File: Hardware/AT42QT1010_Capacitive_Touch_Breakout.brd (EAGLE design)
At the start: 25.4 x 33 mm, 28 parts, among them Q1 600mA/40V, U1 AT42QT1010 - UDFN

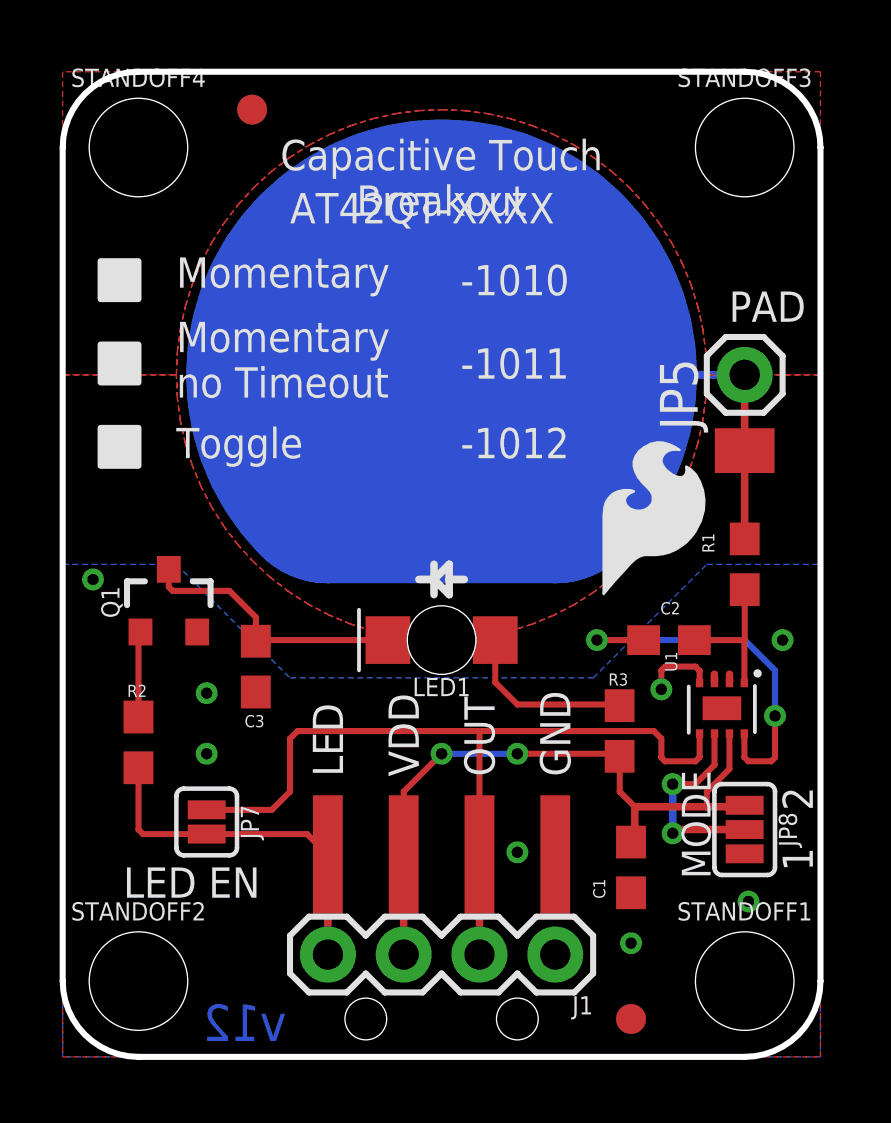
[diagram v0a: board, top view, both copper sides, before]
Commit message: Issues from double check Fixed
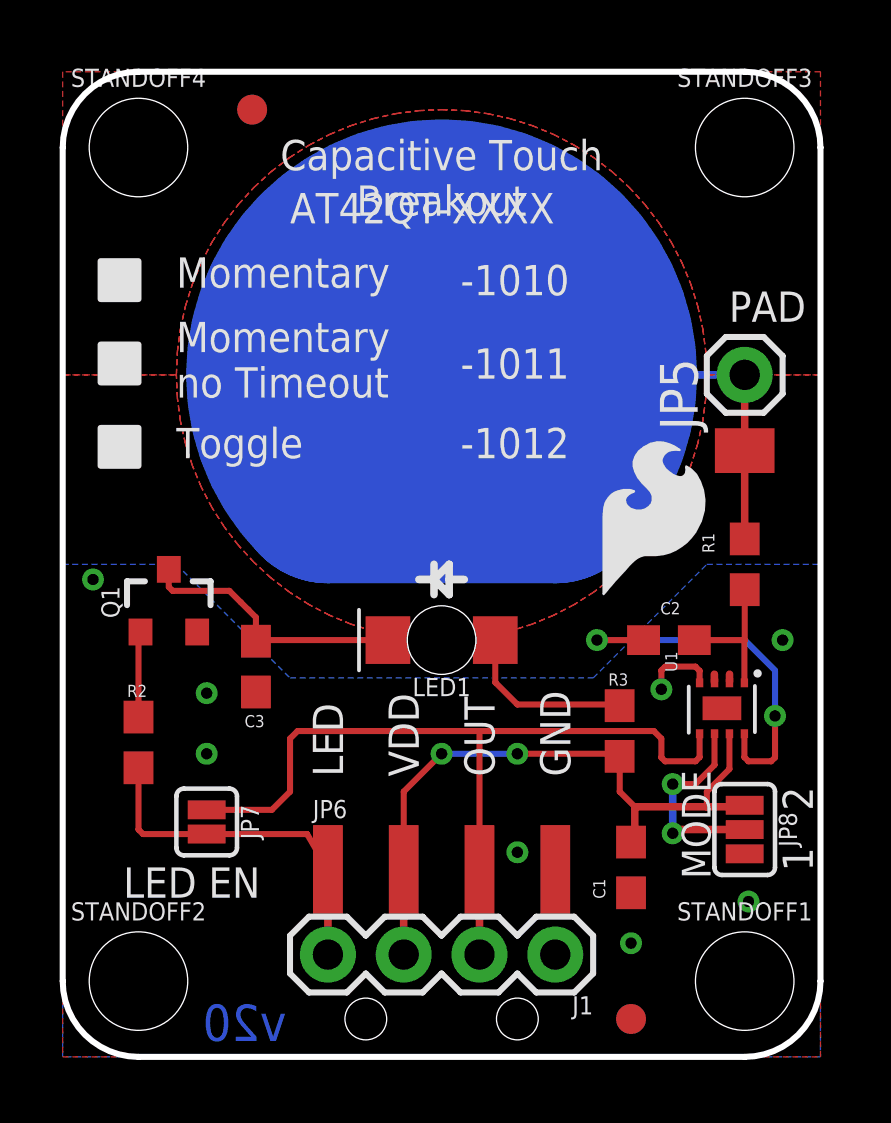
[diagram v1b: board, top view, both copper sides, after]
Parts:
- JP6: device SparkFun-Connectors:1X04_SMD_LONG -> SparkFun-Connectors:1X04_SMD_RA_MALE
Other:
- board text added: "v20"
- board text removed: "v12"
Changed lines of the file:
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@@
 <layer number="20" name="Dimension" color="15" fill="1" visible="yes" active="yes"/>
 <layer number="21" name="tPlace" color="16" fill="1" visible="yes" active="yes"/>
-<layer number="22" name="bPlace" color="14" fill="1" visible="no" active="yes"/>
+<layer number="22" name="bPlace" color="14" fill="1" visible="yes" active="yes"/>
 <layer number="23" name="tOrigins" color="15" fill="1" visible="yes" active="yes"/>
 <layer number="24" name="bOrigins" color="15" fill="1" visible="yes" active="yes"/>
@@
 <layer number="47" name="Measures" color="7" fill="1" visible="no" active="yes"/>
 <layer number="48" name="Document" color="7" fill="1" visible="no" active="yes"/>
-<layer number="49" name="Reference" color="7" fill="1" visible="yes" active="yes"/>
+<layer number="49" name="Reference" color="7" fill="1" visible="no" active="yes"/>
 <layer number="50" name="dxf" color="7" fill="1" visible="no" active="yes"/>
 <layer number="53" name="tGND_GNDA" color="7" fill="9" visible="no" active="no"/>
@@
 <text x="13.97" y="5.08" size="1.016" layer="22" font="vector" ratio="15" rot="MR270" align="center-right">OUT</text>
 <text x="16.51" y="5.08" size="1.016" layer="22" font="vector" ratio="15" rot="MR270" align="center-right">GND</text>
-<text x="6.096" y="1.143" size="1.2192" layer="16" font="vector" ratio="15" rot="MR0" align="center">v12</text>
+<text x="6.096" y="1.143" size="1.2192" layer="16" font="vector" ratio="15" rot="MR0" align="center">v20</text>
 <text x="22.86" y="24.638" size="1.016" layer="22" font="vector" ratio="15" rot="MR270" align="center-right">PAD</text>
 <text x="12.7" y="28.194" size="1.016" layer="21" font="vector" ratio="19" align="bottom-center">Capacitive Touch
@@
 <attribute name="VALUE" x="21.59" y="19.685" size="1.27" layer="27"/>
 </element>
-<element name="JP6" library="SparkFun-Connectors" package="1X04_SMD_LONG" value="SMD" x="12.7" y="1.27">
+<element name="JP6" library="SparkFun-Connectors" package="1X04_SMD_RA_MALE" value="SMD" x="12.7" y="1.27">
 <attribute name="SF_ID" value="PRT-12638" x="12.7" y="1.27" size="1.778" layer="27" display="off"/>
 <attribute name="PROD_ID" value="CONN-09140" x="12.7" y="1.27" size="1.778" layer="27" display="off"/>
@@
 <wire x1="22.8092" y1="8.382" x2="22.86" y2="8.4328" width="0.254" layer="1"/>
 <contactref element="J1" pad="3"/>
-<wire x1="11.43" y1="3.429" x2="11.43" y2="6.77" width="0.254" layer="1"/>
+<wire x1="11.43" y1="3.429" x2="11.43" y2="6.27" width="0.254" layer="1"/>
 <wire x1="21.59" y1="8.89" x2="21.59" y2="8.382" width="0.2032" layer="1"/>
 <wire x1="18.669" y1="10.072" x2="18.669" y2="8.89" width="0.2032" layer="1"/>
-<wire x1="11.43" y1="6.77" x2="11.43" y2="8.89" width="0.2032" layer="1"/>
+<wire x1="11.43" y1="6.27" x2="11.43" y2="8.89" width="0.2032" layer="1"/>
 <wire x1="11.43" y1="8.89" x2="12.7" y2="10.16" width="0.2032" layer="1"/>
 <via x="12.7" y="10.16" extent="1-16" drill="0.381"/>
@@
 <contactref element="JP7" pad="1"/>
 <contactref element="J1" pad="2"/>
-<wire x1="13.97" y1="6.77" x2="13.97" y2="3.429" width="0.254" layer="1"/>
+<wire x1="13.97" y1="6.27" x2="13.97" y2="3.429" width="0.254" layer="1"/>
 <wire x1="4.826" y1="8.2804" x2="7.0104" y2="8.2804" width="0.2032" layer="1"/>
 <wire x1="7.62" y1="8.89" x2="7.62" y2="10.668" width="0.2032" layer="1"/>
-<wire x1="13.97" y1="10.922" x2="13.97" y2="6.77" width="0.2032" layer="1"/>
+<wire x1="13.97" y1="10.922" x2="13.97" y2="6.27" width="0.2032" layer="1"/>
 <wire x1="19.812" y1="10.922" x2="13.97" y2="10.922" width="0.2032" layer="1"/>
 <wire x1="7.62" y1="10.668" x2="7.874" y2="10.922" width="0.2032" layer="1"/>
@@
 <contactref element="J1" pad="4"/>
 <wire x1="8.89" y1="3.81" x2="8.89" y2="3.429" width="0.254" layer="16"/>
-<wire x1="8.89" y1="6.77" x2="8.89" y2="3.429" width="0.254" layer="1"/>
-<wire x1="8.6224" y1="6.5024" x2="8.89" y2="6.77" width="0.2032" layer="1"/>
+<wire x1="8.89" y1="6.27" x2="8.89" y2="3.429" width="0.254" layer="1"/>
+<wire x1="8.6224" y1="6.5024" x2="8.89" y2="6.27" width="0.2032" layer="1"/>
 <wire x1="4.6736" y1="7.62" x2="4.826" y2="7.4676" width="0.2032" layer="1"/>
 <wire x1="4.826" y1="7.4676" x2="2.6924" y2="7.4676" width="0.2032" layer="1"/>
@@
 <wire x1="2.54" y1="7.62" x2="2.54" y2="9.691" width="0.2032" layer="1"/>
 <wire x1="4.826" y1="7.4676" x2="8.1924" y2="7.4676" width="0.2032" layer="1"/>
-<wire x1="8.1924" y1="7.4676" x2="8.89" y2="6.77" width="0.2032" layer="1"/>
+<wire x1="8.1924" y1="7.4676" x2="8.89" y2="6.27" width="0.2032" layer="1"/>
 </signal>
 <signal name="N$4">

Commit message: Update for REDS review
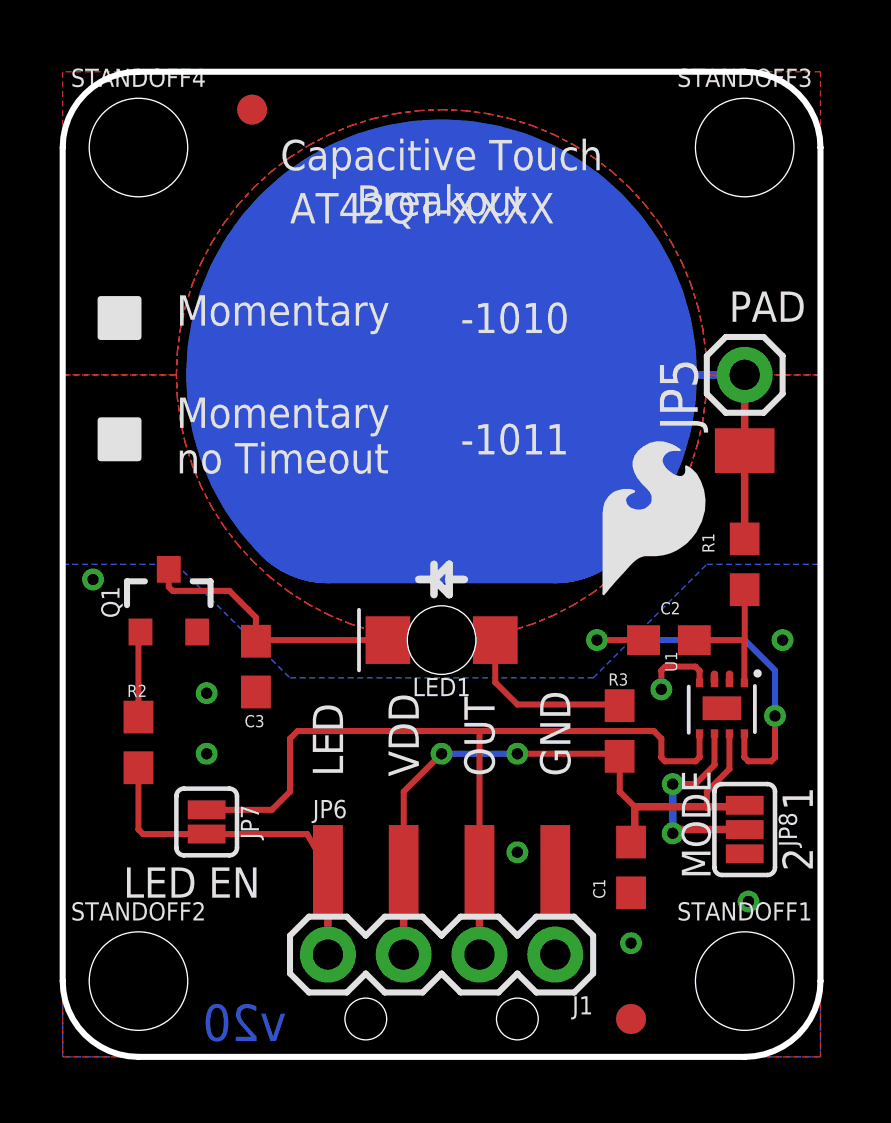
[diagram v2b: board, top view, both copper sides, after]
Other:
- board text removed: "-1012"
- board text removed: "Toggle"
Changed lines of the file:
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@@
 <layer number="47" name="Measures" color="7" fill="1" visible="no" active="yes"/>
 <layer number="48" name="Document" color="7" fill="1" visible="no" active="yes"/>
-<layer number="49" name="Reference" color="7" fill="1" visible="no" active="yes"/>
+<layer number="49" name="Reference" color="7" fill="1" visible="yes" active="yes"/>
 <layer number="50" name="dxf" color="7" fill="1" visible="no" active="yes"/>
 <layer number="53" name="tGND_GNDA" color="7" fill="9" visible="no" active="no"/>
@@
 <rectangle x1="21.971" y1="14.351" x2="22.352" y2="14.859" layer="41"/>
 <rectangle x1="7.62" y1="7.874" x2="8.001" y2="8.382" layer="41"/>
-<text x="3.81" y="25.781" size="1.016" layer="21" font="vector" ratio="15">Momentary</text>
-<text x="3.81" y="20.066" size="1.016" layer="21" font="vector" ratio="15">Toggle</text>
-<text x="3.81" y="22.098" size="1.016" layer="21" font="vector" ratio="15">Momentary
+<text x="3.81" y="24.511" size="1.016" layer="21" font="vector" ratio="15">Momentary</text>
+<text x="3.81" y="19.558" size="1.016" layer="21" font="vector" ratio="15">Momentary
 no Timeout</text>
-<text x="13.335" y="22.733" size="1.016" layer="21" font="vector" ratio="15">-1011</text>
-<text x="13.335" y="25.527" size="1.016" layer="21" font="vector" ratio="15">-1010</text>
-<text x="13.335" y="20.066" size="1.016" layer="21" font="vector" ratio="15">-1012</text>
+<text x="13.335" y="20.193" size="1.016" layer="21" font="vector" ratio="15">-1011</text>
+<text x="13.335" y="24.257" size="1.016" layer="21" font="vector" ratio="15">-1010</text>
 <text x="7.62" y="27.94" size="1.016" layer="21" font="vector" ratio="15">AT42QT-XXXX</text>
 <text x="21.717" y="5.969" size="0.9652" layer="21" font="vector" ratio="15" rot="R90">MODE</text>
-<text x="25.146" y="6.223" size="1.016" layer="21" font="vector" ratio="15" rot="R90">1</text>
-<text x="25.146" y="8.255" size="1.016" layer="21" font="vector" ratio="15" rot="R90">2</text>
+<text x="25.146" y="8.255" size="1.016" layer="21" font="vector" ratio="15" rot="R90">1</text>
+<text x="25.146" y="6.223" size="1.016" layer="21" font="vector" ratio="15" rot="R90">2</text>
 <polygon width="0.2032" layer="21">
-<vertex x="1.27" y="26.67"/>
 <vertex x="1.27" y="25.4"/>
+<vertex x="1.27" y="24.13"/>
+<vertex x="2.54" y="24.13"/>
 <vertex x="2.54" y="25.4"/>
-<vertex x="2.54" y="26.67"/>
 </polygon>
 <polygon width="0.2032" layer="21">
-<vertex x="1.27" y="23.876"/>
-<vertex x="1.27" y="22.606"/>
-<vertex x="2.54" y="22.606"/>
-<vertex x="2.54" y="23.876"/>
-</polygon>
-<polygon width="0.2032" layer="21">
-<vertex x="1.27" y="21.082"/>
-<vertex x="1.27" y="19.812"/>
-<vertex x="2.54" y="19.812"/>
-<vertex x="2.54" y="21.082"/>
+<vertex x="1.27" y="21.336"/>
+<vertex x="1.27" y="20.066"/>
+<vertex x="2.54" y="20.066"/>
+<vertex x="2.54" y="21.336"/>
 </polygon>
 </plain>

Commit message: Minor adjustment before double check
Moved fiducials so that it does not overlay silk, adjusted the "PAD"
silk to be better aligned with the through hole.
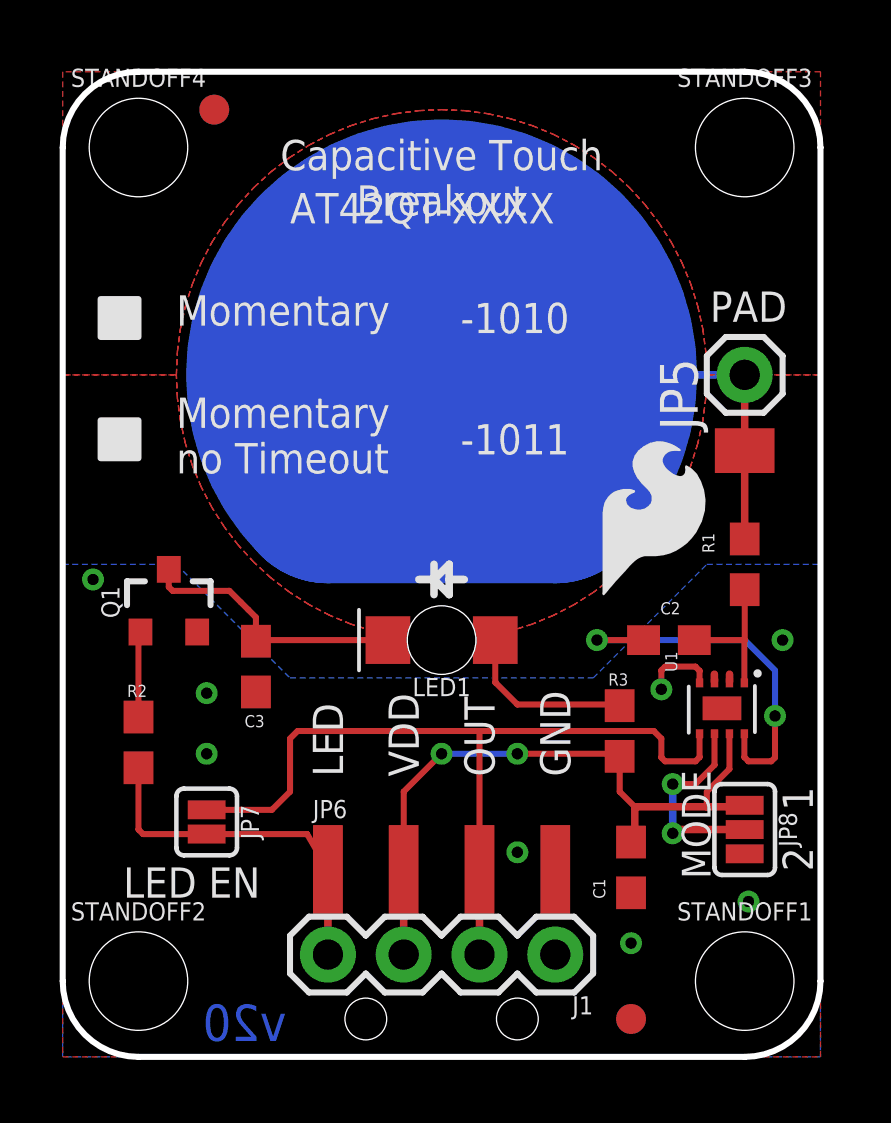
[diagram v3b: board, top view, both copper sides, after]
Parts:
- moved FID1 1.27 mm to (5.08, 31.8)
- moved FID4 1.27 mm to (5.08, 31.8)
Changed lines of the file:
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@@
 <rectangle x1="0" y1="30.48" x2="2.54" y2="33.02" layer="41"/>
 <rectangle x1="22.86" y1="30.48" x2="25.4" y2="33.02" layer="41"/>
-<text x="23.622" y="24.638" size="1.016" layer="21" font="vector" ratio="19" rot="R180" align="top-center">PAD</text>
+<text x="22.987" y="24.638" size="1.016" layer="21" font="vector" ratio="19" rot="R180" align="top-center">PAD</text>
 <text x="8.89" y="9.398" size="1.016" layer="21" font="vector" ratio="15" rot="R90" align="center-left">LED</text>
 <text x="11.43" y="9.398" size="1.016" layer="21" font="vector" ratio="15" rot="R90" align="center-left">VDD</text>
@@
 <attribute name="VALUE" value="Green" x="12.7" y="13.97" size="1.778" layer="27" rot="R180" display="off"/>
 </element>
-<element name="FID1" library="SparkFun-Aesthetics" package="FIDUCIAL-1X2" value="FIDUCIAL1X2" x="6.35" y="31.75"/>
+<element name="FID1" library="SparkFun-Aesthetics" package="FIDUCIAL-1X2" value="FIDUCIAL1X2" x="5.08" y="31.75"/>
 <element name="FID2" library="SparkFun-Aesthetics" package="FIDUCIAL-1X2" value="FIDUCIAL1X2" x="19.05" y="1.27"/>
 <element name="JP9" library="SparkFun-Connectors" package="PAD-1.5X4.5" value="M01SMD-4.5X1.5" x="22.86" y="20.32" smashed="yes" rot="R90"/>
 <element name="JP8" library="SparkFun-Jumpers" package="SMT-JUMPER_3_NO_SILK" value="JUMPER-SMT_3_NO_SILK" x="22.86" y="7.62" rot="R270"/>
 <element name="FID3" library="SparkFun-Aesthetics" package="FIDUCIAL-1X2" value="FIDUCIAL1X2" x="19.05" y="1.27" rot="MR0"/>
-<element name="FID4" library="SparkFun-Aesthetics" package="FIDUCIAL-1X2" value="FIDUCIAL1X2" x="6.35" y="31.75" rot="MR0"/>
+<element name="FID4" library="SparkFun-Aesthetics" package="FIDUCIAL-1X2" value="FIDUCIAL1X2" x="5.08" y="31.75" rot="MR0"/>
 <element name="JP7" library="SparkFun-Jumpers" package="SMT-JUMPER_2_NO_SILK" value="JUMPER-SMT_2_NO_SILK" x="4.826" y="7.874" rot="R270"/>
 <element name="U$1" library="SparkFun-Aesthetics" package="ORDERING_INSTRUCTIONS" value="SPECIAL_INSTRUCTIONS-ORDERING" x="-35.56" y="-21.59"/>
